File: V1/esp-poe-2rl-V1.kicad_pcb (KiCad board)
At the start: 4 copper layers, 88 x 45 mm, 95 parts, among them J1 USB_C_Receptacle_USB2.0, J2 RJ45 JACK, J3 1x2P 5,08mm, J4 1x2P 5,08mm, K1 G5NB-1A-E-DC5, K2 G5NB-1A-E-DC5, Q1 UMH3N, Q2 WPM2015-3/TR, Q3 LMUN2211LT1G, Q4 MMBT2222A, Q5 MMBT2222A, SW1 RESET, U1 TPS2376DDAR-H, U2 TX4138, U3 SY8089A1AAC, U4 CH340C, U5 ESP32-WROOM-32UE-N16, U6 LAN8710A, U7 AHT20

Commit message: Fabrication updates
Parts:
- U7: value AHT20 -> SHT31-DIS; footprint Tales:DFN-6-3x3mm_P1mm -> Tales:Sensirion_DFN-8-1EP_2.5x2.5mm_P0.5mm_EP1.1x1.7mm
- moved R31 2.27 mm to (104.0, 84.8), turned to 90 degrees
- moved R32 2.27 mm to (104.0, 82.5), turned to -90 degrees
- moved C26 1.09 mm to (82.7, 82.0), turned to 180 degrees
- moved U7 0.39 mm to (81.7, 76.4), turned to 0 degrees
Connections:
- R31 pad 2: I2C_SCL -> I2C_SDA
- R32 pad 2: I2C_SDA -> I2C_SCL
- U7 pad 1: unconnected-(U7-NC-Pad1) -> I2C_SDA
- U7 pad 2: +3.3V -> GND
- U7 pad 3: I2C_SCL -> unconnected-(U7-ALERT-Pad3)
- U7 pad 4: I2C_SDA -> I2C_SCL
- U7 pad 5: GND -> +3.3V
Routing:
- net +3.3V: track 141.7 -> 139.4 mm, vias 8 -> 6
- net GND: track 73.7 -> 75.5 mm, vias 41 -> 39
- net /EMAC_TXD0: track 24.4 -> 25.8 mm
- net I2C_SCL: track 32.7 -> 33.4 mm
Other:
- outline, holes or cut-outs redrawn

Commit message: Fabrication updates
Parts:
- D5, D7, D8: value EMERALD -> WHITE
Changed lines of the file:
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@@
 			)
 		)
-		(property "Package" "1206"
+		(property "Package" "1206/3216"
 			(at 301.2 170 0)
 			(layer "F.Fab")
@@
 			)
 		)
-		(property "Value" "EMERALD"
+		(property "Value" "WHITE"
 			(at 0 1.43 0)
 			(layer "F.Fab")
@@
 			)
 		)
-		(property "LCSC Part #" "C2984266"
+		(property "LCSC Part #" "C2290"
 			(at 0 0 0)
 			(layer "F.Fab")
@@
 			)
 		)
-		(property "Mfr" "Everlight eLEC"
+		(property "Mfr" "Hubei KENTO Elec"
 			(at 0 0 0)
 			(layer "F.Fab")
@@
 			)
 		)
-		(property "Mfr PN" "19-213/GHC-XS1T1/5T"
+		(property "Mfr PN" "KT-0603W"
 			(at 0 0 0)
 			(layer "F.Fab")
@@
 			)
 		)
-		(property "Package" "0603"
+		(property "Package" "0603/1608"
 			(at 0 0 0)
 			(layer "F.Fab")
@@
 			)
 		)
-		(property "Vendor PN" "C2984266"
+		(property "Vendor PN" "C2290"
 			(at 0 0 0)
 			(layer "F.Fab")
@@
 			)
 		)
-		(property "Value" "EMERALD"
+		(property "Value" "WHITE"
 			(at 0 1.43 0)
 			(layer "F.Fab")
@@
 			)
 		)
-		(property "LCSC Part #" "C2984266"
+		(property "LCSC Part #" "C2290"
 			(at 190.575 156 0)
 			(layer "F.Fab")
@@
 			)
 		)
-		(property "Mfr" "Everlight eLEC"
+		(property "Mfr" "Hubei KENTO Elec"
 			(at 190.575 156 0)
 			(layer "F.Fab")
@@
 			)
 		)
-		(property "Mfr PN" "19-213/GHC-XS1T1/5T"
+		(property "Mfr PN" "KT-0603W"
 			(at 190.575 156 0)
 			(layer "F.Fab")
@@
 			)
 		)
-		(property "Package" "0603"
+		(property "Package" "0603/1608"
 			(at 190.575 156 0)
 			(layer "F.Fab")
@@
 			)
 		)
-		(property "Vendor PN" "C2984266"
+		(property "Vendor PN" "C2290"
 			(at 190.575 156 0)
 			(layer "F.Fab")
@@
 			)
 		)
-		(property "Value" "EMERALD"
+		(property "Value" "WHITE"
 			(at 0 1.43 0)
 			(layer "F.Fab")
@@
 			)
 		)
-		(property "LCSC Part #" "C2984266"
+		(property "LCSC Part #" "C2290"
 			(at 164.575 156 0)
 			(layer "F.Fab")
@@
 			)
 		)
-		(property "Mfr" "Everlight eLEC"
+		(property "Mfr" "Hubei KENTO Elec"
 			(at 164.575 156 0)
 			(layer "F.Fab")
@@
 			)
 		)
-		(property "Mfr PN" "19-213/GHC-XS1T1/5T"
+		(property "Mfr PN" "KT-0603W"
 			(at 164.575 156 0)
 			(layer "F.Fab")
@@
 			)
 		)
-		(property "Package" "0603"
+		(property "Package" "0603/1608"
 			(at 164.575 156 0)
 			(layer "F.Fab")
@@
 			)
 		)
-		(property "Vendor PN" "C2984266"
+		(property "Vendor PN" "C2290"
 			(at 164.575 156 0)
 			(layer "F.Fab")

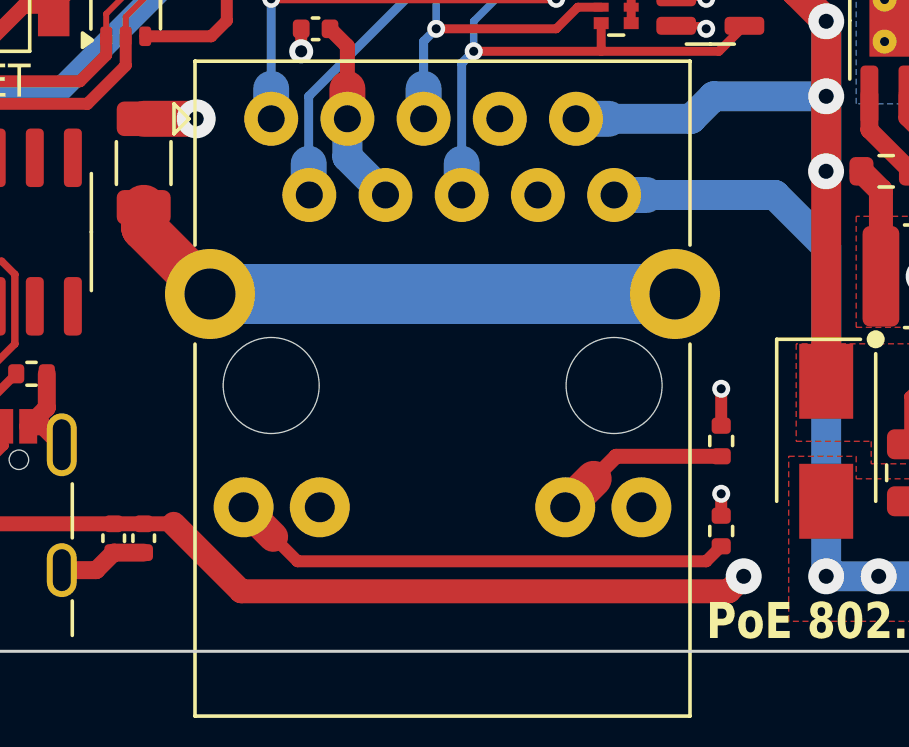
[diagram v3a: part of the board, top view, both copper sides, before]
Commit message: Corrected leds connections on RJ45 jack
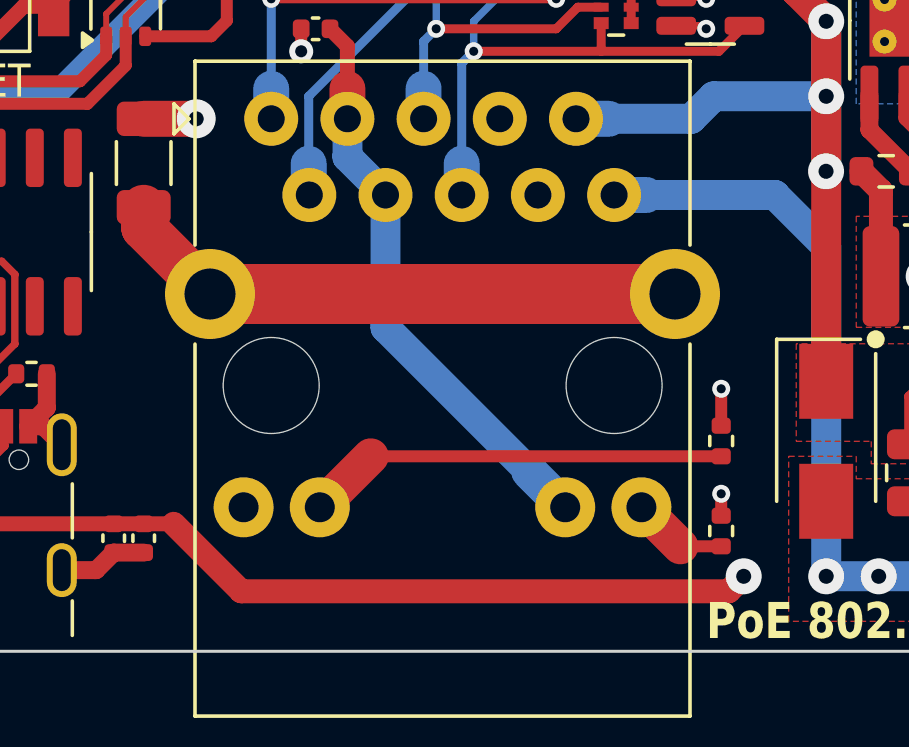
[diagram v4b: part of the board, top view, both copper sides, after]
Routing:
- net Net-(J2-RLED-): track 16.9 -> 3.20 mm
- net /LED_Y_A: track 27.0 -> 40.3 mm
- net Net-(J2-LLED-): track 5.90 -> 14.1 mm
- net +3.3VA: track 61.7 -> 63.2 mm
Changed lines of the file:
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@@
 		)
 		(pad "11" thru_hole circle
-			(at 12.34 12.95)
+			(at -0.92 12.95)
 			(size 2 2)
 			(drill 1)
@@
 		)
 		(pad "12" thru_hole circle
-			(at 9.8 12.95)
+			(at 1.62 12.95)
 			(size 2 2)
 			(drill 1)
@@
 		)
 		(pad "13" thru_hole circle
-			(at 1.62 12.95)
+			(at 9.8 12.95)
 			(size 2 2)
 			(drill 1)
@@
 		)
 		(pad "14" thru_hole circle
-			(at -0.92 12.95)
+			(at 12.34 12.95)
 			(size 2 2)
 			(drill 1)
@@
 	)
 	(segment
+		(start 125.81 105.21)
+		(end 130.6 110)
+		(width 1)
+		(layer "B.Cu")
+		(net 14)
+	)
+	(segment
 		(start 133.75 91.75)
 		(end 126.5 91.75)
@@
 	)
 	(segment
+		(start 131.8 111.2)
+		(end 130.6 110)
+		(width 1.2)
+		(layer "B.Cu")
+		(net 14)
+	)
+	(segment
+		(start 125.81 100.79)
+		(end 125.81 105.21)
+		(width 1)
+		(layer "B.Cu")
+		(net 14)
+	)
+	(segment
 		(start 126.5 91.75)
 		(end 126 91.25)
@@
 	)
 	(segment
-		(start 123.62 111.2)
-		(end 124.82 110)
-		(width 1.2)
-		(layer "In2.Cu")
-		(net 14)
-	)
-	(segment
 		(start 128 77.25)
 		(end 127 78.25)
@@
 	)
 	(segment
-		(start 125.81 100.79)
-		(end 125.81 109.01)
-		(width 1)
-		(layer "In2.Cu")
-		(net 14)
-	)
-	(segment
 		(start 127 90.25)
 		(end 126 91.25)
@@
 	)
 	(segment
-		(start 125.81 109.01)
-		(end 124.82 110)
-		(width 1)
-		(layer "In2.Cu")
-		(net 14)
-	)
-	(segment
 		(start 131.75 82)
 		(end 132.5 82)
@@
 	)
 	(segment
+		(start 119.96 104.09)
+		(end 135.46 104.09)
+		(width 2)
+		(layer "F.Cu")
+		(net 16)
+	)
+	(segment
 		(start 117.75 101.2)
 		(end 117.75 101.88)
@@
 	)
 	(segment
-		(start 119.96 104.09)
-		(end 135.46 104.09)
-		(width 2)
-		(layer "B.Cu")
-		(net 16)
-	)
-	(segment
 		(start 135.5 74.77)
 		(end 135.5 75.75)
@@
 	)
 	(segment
-		(start 136.5 113)
-		(end 137 112.5)
-		(width 0.4)
+		(start 135.64 112.5)
+		(end 134.34 111.2)
+		(width 1.2)
 		(layer "F.Cu")
 		(net 34)
 	)
 	(segment
-		(start 122.88 113)
-		(end 122.065 112.185)
+		(start 135.64 112.5)
+		(end 137 112.5)
 		(width 0.4)
 		(layer "F.Cu")
@@
 	)
 	(segment
-		(start 122.88 113)
-		(end 136.5 113)
+		(start 137 109.5)
+		(end 125.32 109.5)
 		(width 0.4)
 		(layer "F.Cu")
-		(net 34)
-	)
-	(segment
-		(start 121.08 111.2)
-		(end 122.065 112.185)
-		(width 1)
-		(layer "F.Cu")
-		(net 34)
-	)
-	(segment
-		(start 133.5 109.5)
-		(end 137 109.5)
-		(width 0.5)
-		(layer "F.Cu")
 		(net 35)
 	)
 	(segment
-		(start 131.8 111.2)
-		(end 132.75 110.25)
+		(start 123.62 111.2)
+		(end 125.32 109.5)
 		(width 1.2)
 		(layer "F.Cu")
@@
 	)
 	(segment
-		(start 133.5 109.5)
-		(end 132.75 110.25)
-		(width 0.5)
-		(layer "F.Cu")
-		(net 35)
-	)
-	(segment
 		(start 136.25 89.25)
 		(end 134.645 89.25)
@@
 	)
 	(segment
-		(start 135.5 110.04)
-		(end 134.34 111.2)
+		(start 136.25 89.25)
+		(end 137.25 90.25)
+		(width 0.5)
+		(layer "In2.Cu")
+		(net 36)
+	)
+	(segment
+		(start 121.08 111.2)
+		(end 122.78 109.5)
 		(width 1.2)
 		(layer "In2.Cu")
@@
 	)
 	(segment
-		(start 138 107.54)
-		(end 138 103)
+		(start 138 107.5)
+		(end 136 109.5)
 		(width 0.5)
 		(layer "In2.Cu")
@@
 	)
 	(segment
-		(start 135.5 110.04)
-		(end 138 107.54)
+		(start 136 109.5)
+		(end 122.78 109.5)
 		(width 0.5)
 		(layer "In2.Cu")
@@
 	)
 	(segment
-		(start 137.25 90.25)
-		(end 136.25 89.25)
+		(start 138 103)
+		(end 138 107.5)
 		(width 0.5)
 		(layer "In2.Cu")
@@
 	)
 	(segment
-		(start 138 103)
+		(start 137.25 90.25)
 		(end 137.25 102.25)
 		(width 0.5)
@@
 	(segment
 		(start 137.25 102.25)
-		(end 137.25 90.25)
+		(end 138 103)
 		(width 0.5)
 		(layer "In2.Cu")

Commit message: V1.4
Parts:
- removed C26: 100nF/50V, Tales:C_0402_1005Metric
- removed F1: 500mA, Tales:Fuse_1206_3216Metric
- removed the R31 at (104.0, 84.8)
- removed R32: 2k2/62,5mW, Tales:R_0402_1005Metric
- removed the U4 at (110.9, 102.0)
- removed U7: SHT31-DIS, Tales:Sensirion_DFN-8-1EP_2.5x2.5mm_P0.5mm_EP1.1x1.7mm
- added D1: USBLC6-2SC6, Package_TO_SOT_SMD:SOT-23-6, F.Cu at (115.0, 103.2)
- added U1: CH340K, Package_SO:SSOP-10-1EP_3.9x4.9mm_P1mm_EP2.1x3.3mm, F.Cu at (108.0, 102.2)
- R1: renamed from R23; value 10k/62,5mW -> 10k
- R10: renamed from R30; value 680R/62,5mW -> 680R
- R11: renamed from R16; value 10k/62,5mW -> 10k
- R12: renamed from R17; value 10k/62,5mW -> 10k
- R13: renamed from R33; value 22R/62,5mW -> 22R
- R14: renamed from R18; value 10k/62,5mW -> 10k
- R15: renamed from R19; value 10k/62,5mW -> 10k
- R16: renamed from R20; value 12,1k/62,5mW -> 12,1k
- R17: renamed from R21; value 330R/62,5mW -> 330R
- R18: renamed from R22; value 330R/62,5mW -> 330R
- R2: renamed from R14; value 5,1k/62,5mW -> 5,1k
- R20: renamed from R11; value 820R/100mW -> 1k; footprint Tales:R_0603_1608Metric -> Tales:R_0402_1005Metric
- R21: renamed from R3; value 180k/62,5mW -> 180k
- R22: renamed from R5; value 30,1k/62,5mW -> 30,1k
- R27: renamed from R1; value 130k/62,5mW -> 130k
- R28: renamed from R2; value 10k/62,5mW -> 10k
- R3: renamed from R24; value 1k/62,5mW -> 1k
- R4: renamed from R15; value 5,1k/62,5mW -> 5,1k
- R5: renamed from R25; value 10k/62,5mW -> 10k
- R6: renamed from R28; value 10k/62,5mW -> 10k
- R7: renamed from R26; value 1k/62,5mW -> 1k
- R8: renamed from R29; value 1k/62,5mW -> 1k
- R9: renamed from R27; value 680R/62,5mW -> 680R
- RN1, RN2: value 4x2,2k/62,5mW -> 4x2,2k
- RN3: value 4x49,9R/62,5mW -> 4x49,9R
- moved K1 9.49 mm to (85.5, 89.5)
- moved K2 9.05 mm to (99.0, 89.5)
- moved D2 5.59 mm to (84.8, 75.0)
- moved D4 5.41 mm to (84.2, 77.5)
- moved R5 5.35 mm to (86.8, 73.5)
- moved Q4 5.32 mm to (88.2, 76.5)
- moved R9 5.07 mm to (83.5, 73.5)
- moved R7 4.86 mm to (89.2, 73.5)
- moved J3 4.72 mm to (95.5, 106.5)
- moved R18 4.52 mm to (137.2, 113.5), turned to -90 degrees
- moved J2 4.47 mm to (82.0, 106.5)
- moved R2 4.36 mm to (104.5, 108.5), turned to 90 degrees
- moved R4 3.46 mm to (117.0, 108.5), turned to 90 degrees
- moved R22 3.12 mm to (144.8, 107.8)
- moved C10 2.01 mm to (129.0, 92.5), turned to 180 degrees
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- renumbered C24 to C1, C16 to C10, C17 to C11, C23 to C12, C18 to C13, C19 to C14, C20 to C15, C21 to C16, C1 to C17, C6 to C18, C3 to C19, C10 to C2, C7 to C20, C4 to C21, C8 to C22, C2 to C23, C5 to C24, C9 to C25, C25 to C3, C11 to C4, C12 to C5, C13 to C6, C14 to C7, C15 to C8, C22 to C9, D5 to D10, D2 to D11, D7 to D2, D8 to D3, D9 to D4, D10 to D5, D1 to D7, D3 to D8, D4 to D9, J3 to J2, J4 to J3, J2 to J4, L3 to L1, L1 to L2, L2 to L3, Q2 to Q1, Q3 to Q2, Q1 to Q3, R7 to R19, R4 to R23, R8 to R24, R12 to R25, R13 to R26, R9 to R29, R10 to R30, R6 to R31, U5 to U2, U6 to U3, U2 to U4, U3 to U5, U1 to U6
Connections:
- net +3.3V renamed +3V3
- net +3.3VA renamed +3V3A
- net +3.3VLAN renamed +3V3LAN
- net /EMAC_CLK renamed /EMACCLK
- net /EMAC_MDC renamed /EMACMDC
- net /EMAC_MDIO renamed /EMACMDIO
- net /EMAC_RX renamed /EMACRX
- net /EMAC_RXD0 renamed /EMACRXD0
- net /EMAC_RXD1 renamed /EMACRXD1
- net /EMAC_TXD0 renamed /EMACTXD0
- net /EMAC_TXD1 renamed /EMACTXD1
- net /EMAC_TXEN renamed /EMACTXEN
- net /LED_G_K renamed /ETHLEDG
- net /LED_Y_A renamed /ETHLEDY
- net /RD+ renamed /ETHRXD+
- net /RD- renamed /ETHRXD-
- net /TD+ renamed /ETHTXD+
- net /TD- renamed /ETHTXD-
- net /USB_D+ renamed /USBCD+
- net /USB_D- renamed /USBCD-
- net Net-(C3-Pad1) renamed /POWER/5VBS
- net Net-(D10-A) renamed /OUT2CMD
- net Net-(D2-K) renamed /POWER/5VSW
- net Net-(D5-A) renamed /POWER/PWRON
- net Net-(D7-A) renamed /OUT1ON
- net Net-(D7-K) renamed /OUT1CMD
- net Net-(D8-A) renamed /OUT2ON
- net Net-(J1-CC1) renamed /USBCC1
- net Net-(J1-CC2) renamed /USBCC2
- net Net-(J2-LLED-) renamed /ETHLEDYK
- net Net-(J2-RLED-) renamed /ETHLEDGK
- net Net-(J2-SHIELD) renamed /ETHSH
- net Net-(J3-Pin_1) renamed /OUT1LN
- net Net-(J3-Pin_2) renamed /OUT1LD
- net Net-(J4-Pin_1) renamed /OUT2LN
- net Net-(J4-Pin_2) renamed /OUT2LD
- net Net-(Q1A-B1) renamed /UARTNDTR
- net Net-(Q1A-C1) renamed /ESPEN
- net Net-(Q1A-E1) renamed /UARTNRTS
- net Net-(Q1B-C2) renamed /ESPPROG
- net Net-(Q2-G) renamed /PHYPWRFET
- net Net-(Q3-C) renamed /PHYPWRBJT
- net Net-(Q4-B) renamed /OUT1BJT
- net Net-(Q5-B) renamed /OUT2BJT
- net Net-(R7-Pad2) renamed /POWER/ILIM
- net Net-(RN1-R3.1) renamed /EMACRXD4
- net Net-(RN2-R2.1) renamed /EMACRXD2
- net Net-(RN2-R3.1) renamed /EMACRXD3
- net Net-(RN2-R4.1) renamed /EMACRXCLK
- net Net-(U1-CLASS) renamed /POWER/RCLASS
- net Net-(U1-DET) renamed /POWER/RDET
- net Net-(U1-ILIM) renamed /POWER/RILIM
- net Net-(U1-UVLO) renamed /POWER/VTAP
- net Net-(U2-BS) renamed /POWER/BS
- net Net-(U2-FB) renamed /POWER/5VREF
- net Net-(U3-FB) renamed /POWER/3V3REF
- net Net-(U3-LX) renamed /POWER/3V3SW
- net Net-(U5-IO17) renamed /EMACGPIO
- net Net-(U6-RBIAS) renamed /RBIAS
- net Net-(U6-VDDCR) renamed /VDDCR
- net Net-(U6-~{RST}) renamed /PHYNRST
- net PHY_PWR renamed PHYPWR
- net PoE+ renamed POE+
- net PoE- renamed POE-
- C2 pad 1: Net-(C10-Pad1) -> 5VUSB
- C4 pad 1: Net-(C10-Pad1) -> 5VUSB
- J1 pad A4: Net-(C10-Pad1) -> 5VUSB
- J1 pad A9: Net-(C10-Pad1) -> 5VUSB
- J1 pad B4: Net-(C10-Pad1) -> 5VUSB
- J1 pad B9: Net-(C10-Pad1) -> 5VUSB
- U2 pad 34: Net-(U4-TXD) -> /UARTTXD
- U2 pad 35: Net-(U4-RXD) -> /UARTRXD
- U2 pad 8: I2C_SCL -> unconnected-(U2-IO32-Pad8)
- U2 pad 9: I2C_SDA -> unconnected-(U2-IO33-Pad9)
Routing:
- net +3V3: track 139.4 -> 37.2 mm, vias 6 -> 13
- net Net-(C10-Pad1): track 81.0 -> 0.00 mm, vias 2 -> 0
- net 5VUSB: track 3.25 -> 80.1 mm, vias 0 -> 6
- net +3V3A: track 63.2 -> 25.3 mm, vias 4 -> 5
- net Net-(U4-TXD): track 34.5 -> 0.00 mm, vias 2 -> 0
- net I2C_SDA: track 33.5 -> 0.00 mm
- net I2C_SCL: track 33.4 -> 0.00 mm
- net Net-(U4-RXD): track 33.2 -> 0.00 mm, vias 2 -> 0
- net /EMACMDC: track 26.5 -> 0.00 mm, vias 2 -> 1
- net /EMACTXD1: track 25.9 -> 1.27 mm, vias 2 -> 1
- net /EMACTXD0: track 25.8 -> 2.02 mm, vias 2 -> 1
- net /EMACTXEN: track 23.7 -> 1.81 mm, vias 4 -> 1
- net /ESPEN: track 34.4 -> 12.6 mm, vias 2 -> 0
- net /UARTRXD: track 0.00 -> 20.1 mm, vias 0 -> 1
- net /EMACRXD1: track 32.0 -> 14.5 mm, vias 2 -> 1
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- added copper zone on In2.Cu, net +3V3
- added copper zone on In2.Cu, net +3V3A
- added copper zone on In2.Cu, net +3V3LAN
- added copper zone on In2.Cu, net +5V
- added copper zone on In1.Cu, net POE-
- added copper zone on In2.Cu, net POE-
- removed copper zone on F.Cu, net +5V
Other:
- outline, holes or cut-outs redrawn
- rule pad_to_mask_clearance: 0 -> 0.1
- board text added: "5V"
- board text added: "ESP-POE-2RL V1.4"
- board text removed: "5V OK"
- board text removed: "ESP-POE-2RL V1.3"
